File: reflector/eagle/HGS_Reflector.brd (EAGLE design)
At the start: 100 x 100 mm, 27 parts, among them J1 U.FL, U3 LP2985XX-N

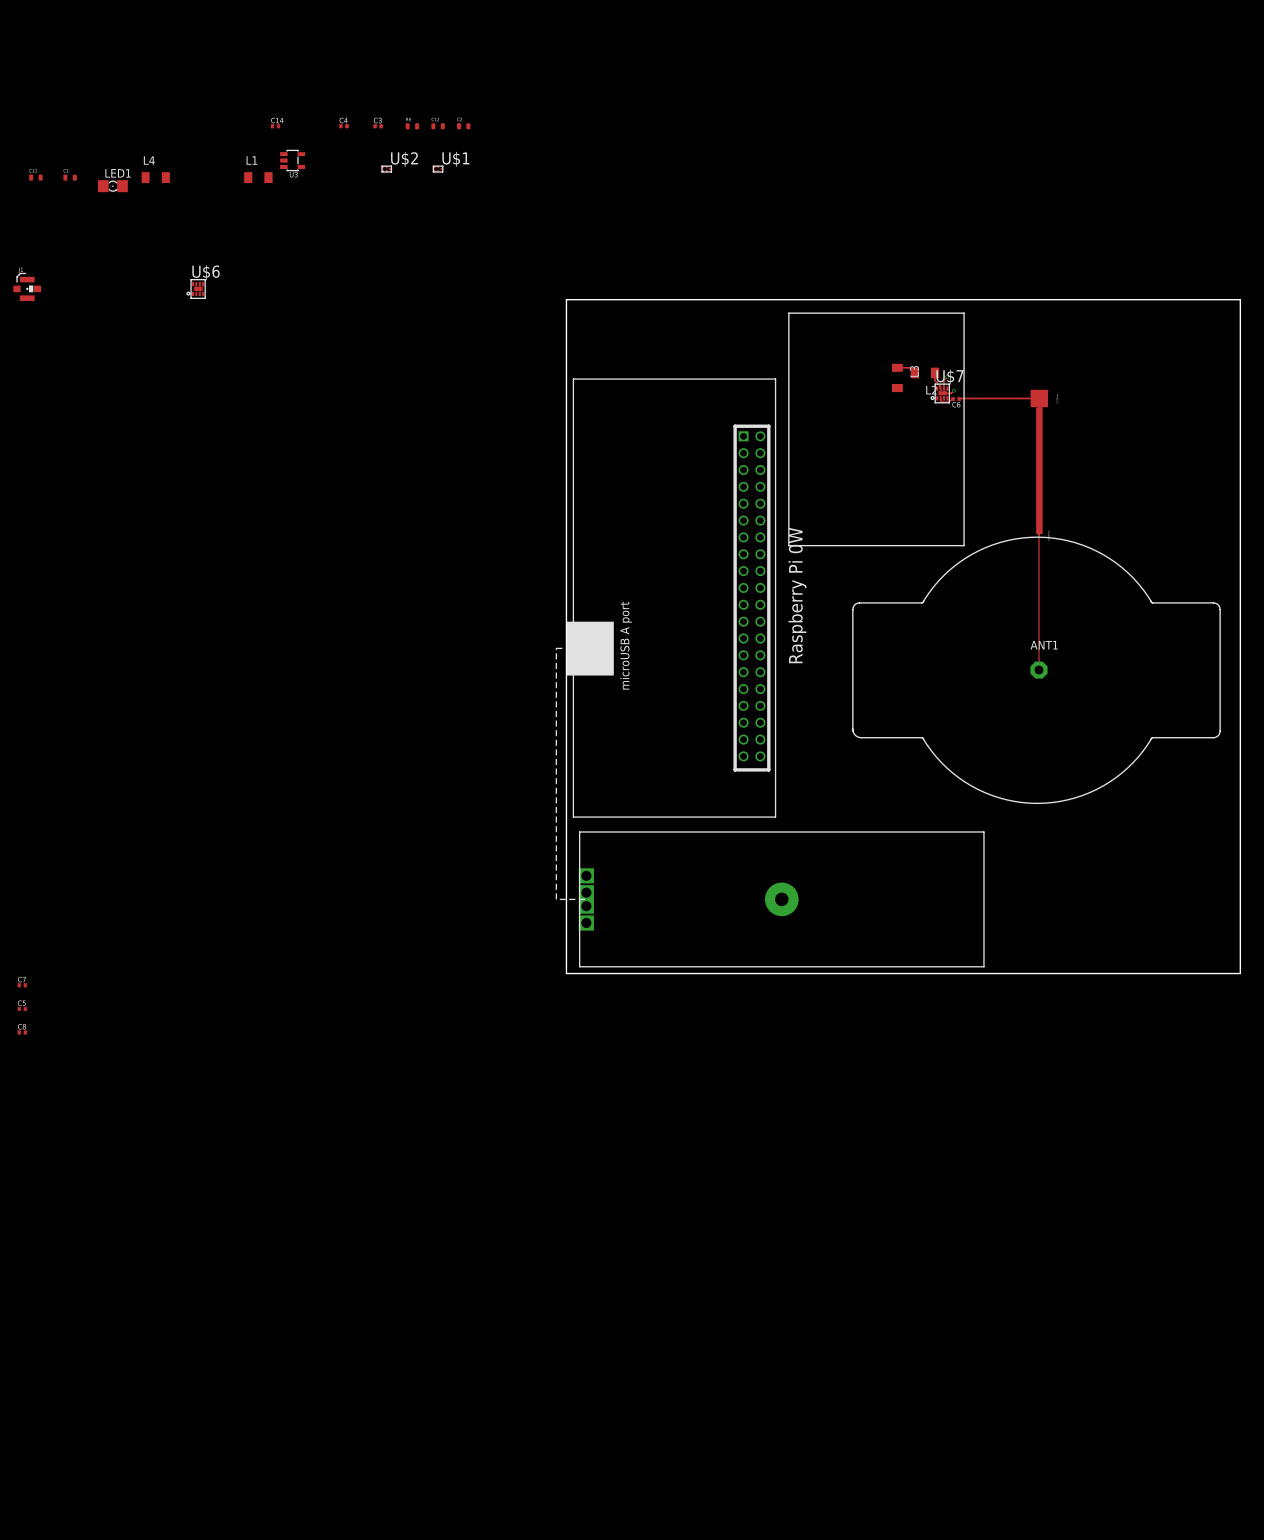
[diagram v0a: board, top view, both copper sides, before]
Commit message: Last Thursday, I updated the HGS board to its actual shape by importing the the DXF file that Marvin Lin sent me. I began work on re-routing the board to fit within the DXF dimensions.
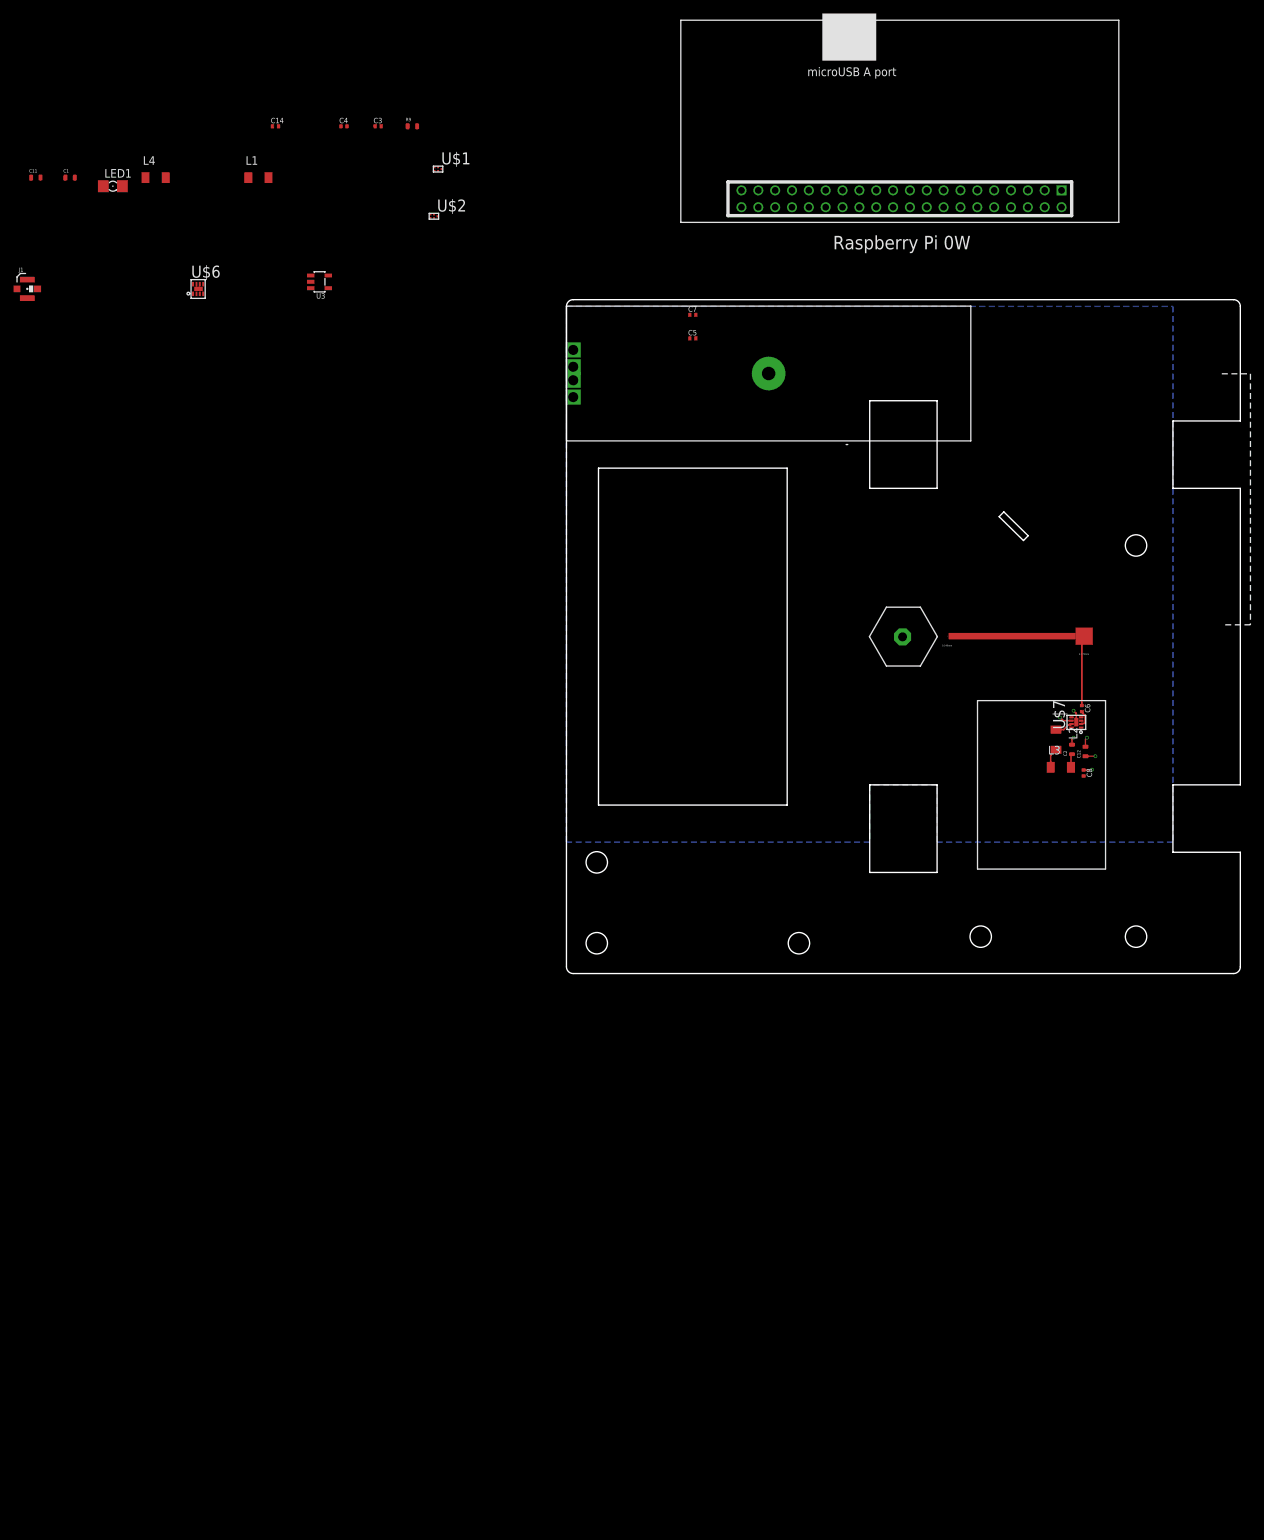
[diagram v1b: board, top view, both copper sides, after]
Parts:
- moved C8 162.1 mm to (76.8, 29.8), turned to 270 degrees
- moved C5 140.7 mm to (18.8, 94.2)
- moved C7 140.7 mm to (18.8, 97.8)
- moved C12 133.6 mm to (77.0, 33.0), turned to 90 degrees
- moved C2 129.2 mm to (75.0, 33.3), turned to 90 degrees
- moved U$5 78.3 mm to (49.5, 126.5), turned to 180 degrees
- moved U$4 78.1 mm to (30.0, 89.0)
- moved L3 62.7 mm to (73.4, 30.6), turned to 0 degrees
- moved L2 57.8 mm to (72.6, 34.7), turned to 270 degrees
- moved U$7 52.7 mm to (75.7, 37.3), turned to 90 degrees
- moved C6 49.6 mm to (76.5, 39.3), turned to 270 degrees
- moved U$3 24.9 mm to (66.1, 50.1), turned to 180 degrees
- moved ANT1 20.8 mm to (49.9, 50.0), flipped to the bottom, turned to 180 degrees
- moved U3 18.4 mm to (-36.6, 102.7)
- moved U$2 9.90 mm to (-19.7, 112.4)
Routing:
- net N$2: track 20.2 -> 0.04 mm, vias 0 -> 1
- net 3.3V: track 0.00 -> 4.76 mm, vias 0 -> 2
- net GND: track 3.74 -> 6.33 mm, vias 2 -> 4
- net N$9: track 11.9 -> 10.4 mm
- added copper zone on layer 15, net 3V
- added copper zone on layer 16, net GND
- added copper zone on layer 2, net GND_TOP
- removed copper zone on layer 15, net GND
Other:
- outline, holes or cut-outs redrawn

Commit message: Cleanup of mechanical stuff; rotated board, imported DXF, reset the dim layer, and put grounds on all layers.
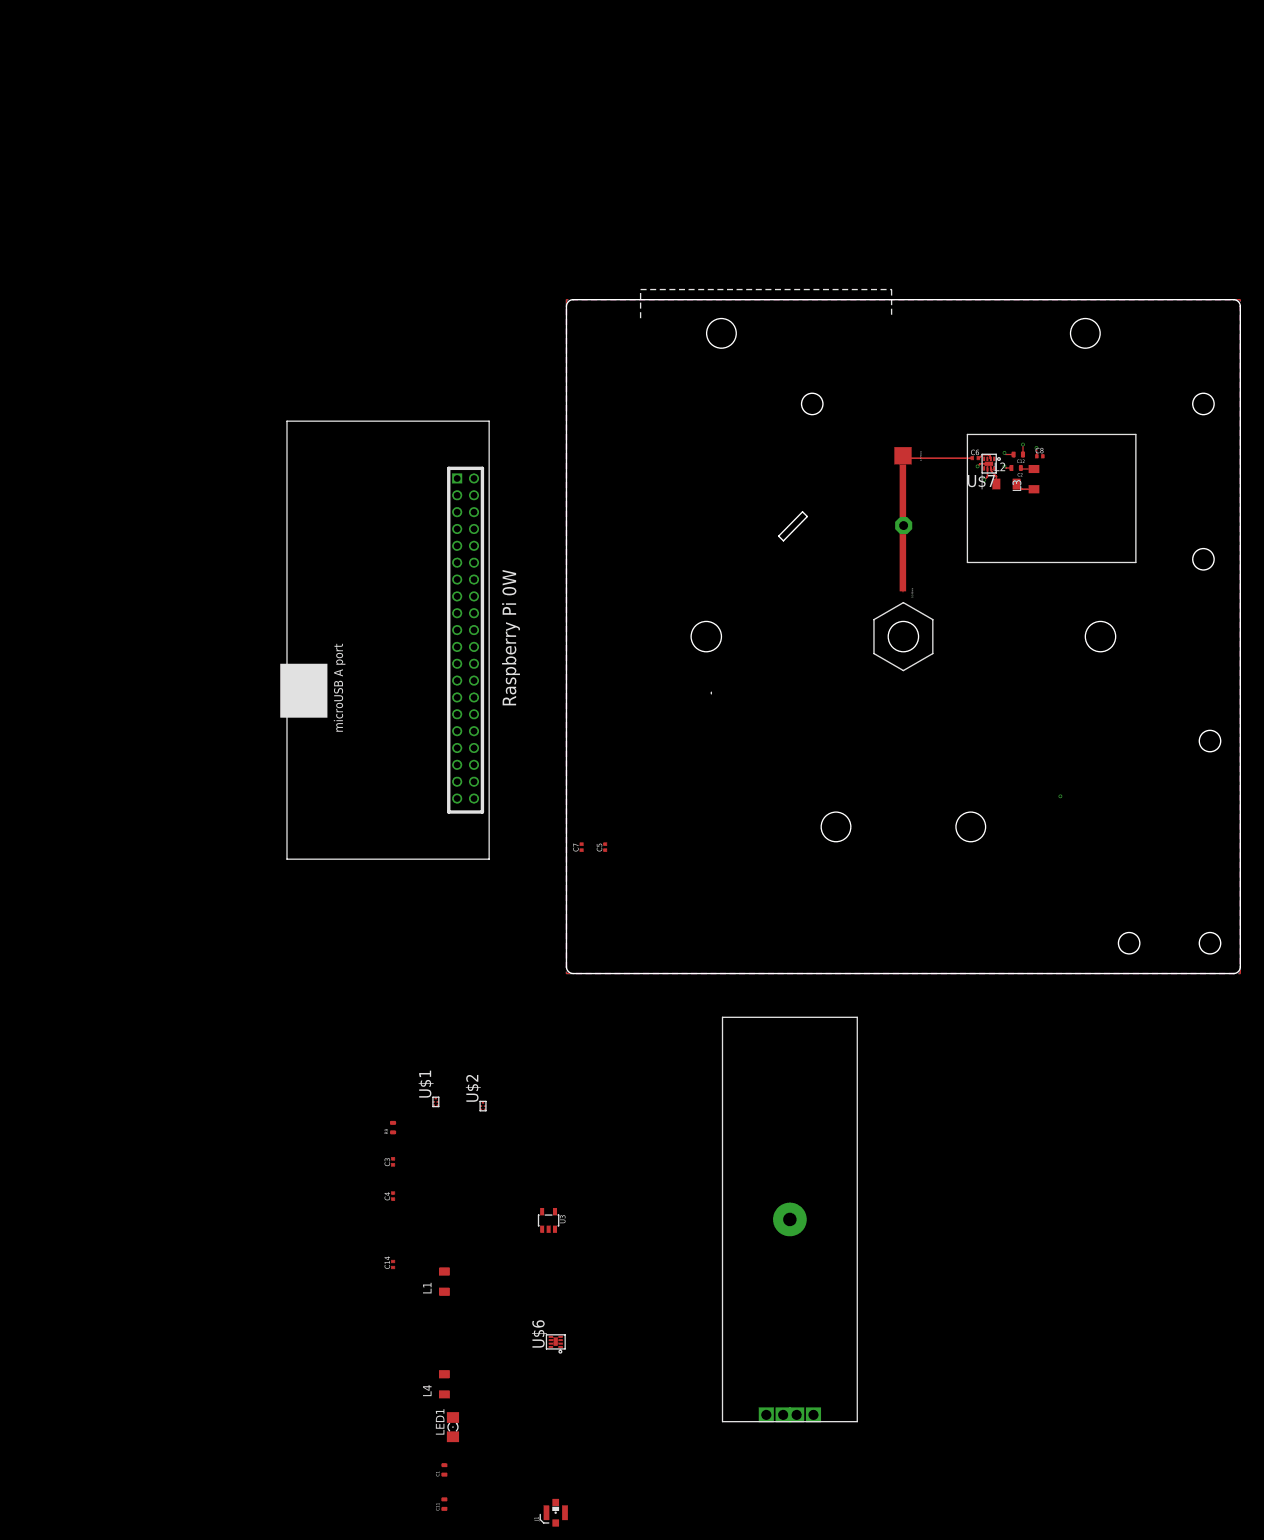
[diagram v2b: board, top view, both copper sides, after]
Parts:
- moved C11 206.0 mm to (-18.1, -78.7), turned to 90 degrees
- moved C1 199.7 mm to (-18.1, -73.7), turned to 90 degrees
- moved J1 197.8 mm to (-1.60, -80.0), turned to 90 degrees
- moved LED1 190.9 mm to (-16.8, -67.3), turned to 90 degrees
- moved L4 184.1 mm to (-18.1, -61.0), turned to 90 degrees
- moved C14 169.8 mm to (-25.7, -43.2), turned to 90 degrees
- moved L1 166.1 mm to (-18.1, -45.7), turned to 90 degrees
- moved U$6 165.0 mm to (-1.60, -54.6), turned to 90 degrees
- moved C4 158.9 mm to (-25.7, -33.0), turned to 90 degrees
- moved C3 153.7 mm to (-25.7, -27.9), turned to 90 degrees
- moved R9 148.6 mm to (-25.7, -22.9), turned to 90 degrees
- moved U3 143.4 mm to (-2.65, -36.6), turned to 90 degrees
- moved U$1 138.4 mm to (-19.4, -19.1), turned to 90 degrees
- moved U$2 132.3 mm to (-12.4, -19.7), turned to 90 degrees
- moved U$4 125.6 mm to (33.2, -36.5), turned to 0 degrees
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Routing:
- net N$2: track 0.04 -> 0.01 mm, vias 1 -> 0
- net GND: vias 4 -> 5
- added copper zone on layer 1, net GND
- added copper zone on layer 15, net GND
- added copper zone on layer 2, net GND
- removed copper zone on layer 2, net GND_TOP
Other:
- outline, holes or cut-outs redrawn

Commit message: With the DXF layer properly configured, I positioned all parts onto the board and completed all of the routing. However, there are a few DRC issues involving details of footprints that need to be changed and connections that did not route properly.
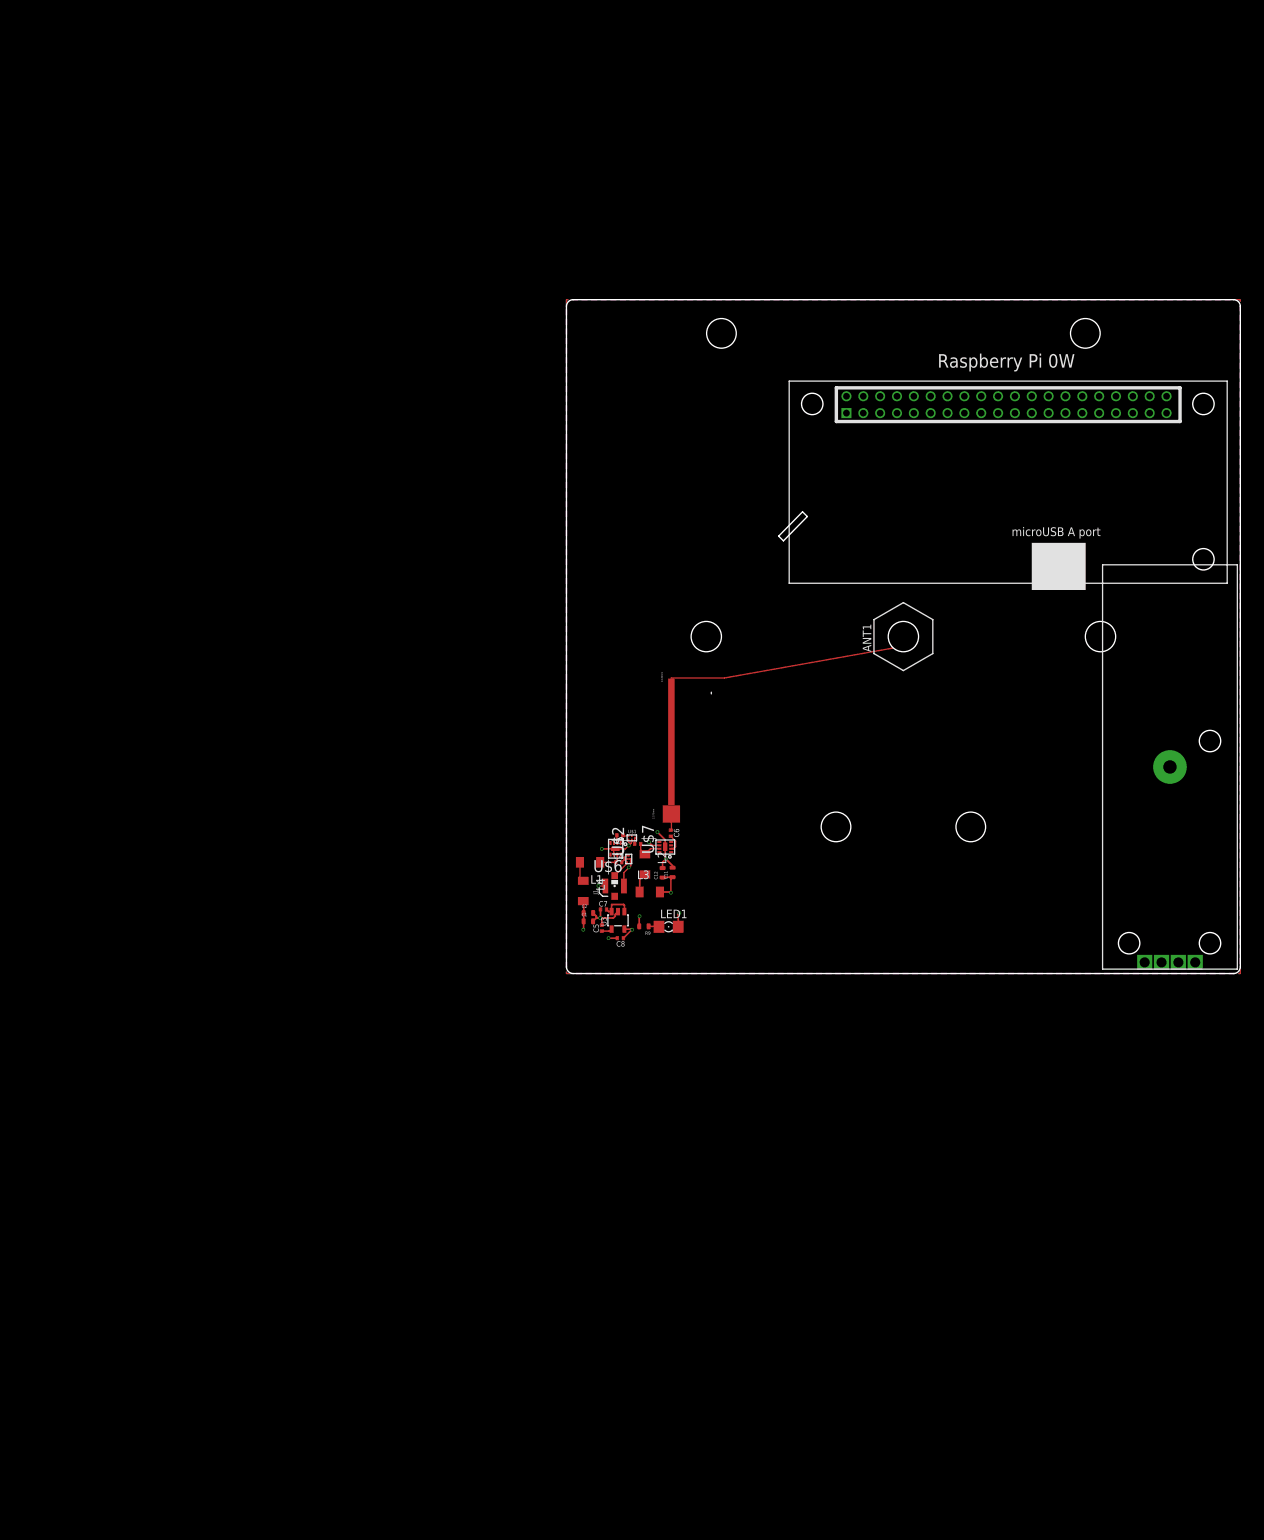
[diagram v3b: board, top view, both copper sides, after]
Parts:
- moved C11 99.7 mm to (15.8, 15.0)
- moved U$5 95.0 mm to (65.6, 72.9), turned to 0 degrees
- moved C8 94.8 mm to (8.00, 5.25), turned to 180 degrees
- moved J1 93.4 mm to (7.15, 13.0)
- moved C2 91.6 mm to (3.26, 8.98), turned to 0 degrees
- moved U$4 87.7 mm to (89.6, 30.7)
- moved C1 84.2 mm to (3.25, 7.75), turned to 0 degrees
- moved L3 83.7 mm to (12.4, 12.1), turned to 0 degrees
- moved C12 81.5 mm to (14.3, 14.9), turned to 90 degrees
- moved LED1 80.9 mm to (15.2, 6.94), turned to 0 degrees
- moved L2 77.9 mm to (11.6, 16.2), turned to 270 degrees
- moved L4 76.1 mm to (2.50, 12.2), turned to 270 degrees
- moved U$7 74.4 mm to (14.7, 18.8), turned to 90 degrees
- moved U$6 73.6 mm to (7.25, 18.5), turned to 180 degrees
- moved C14 72.2 mm to (10.6, 19.2), turned to 180 degrees
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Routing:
- net N$2: track 0.01 -> 35.6 mm
- net GND: track 6.33 -> 33.5 mm, vias 5 -> 10
- net 3.3V: track 4.76 -> 14.6 mm, vias 2 -> 4
- net N$9: track 10.4 -> 2.42 mm
- net 5V: track 0.00 -> 4.81 mm
- net N$13: track 0.00 -> 3.55 mm
- net N$14: track 0.00 -> 2.96 mm
- net N$5: track 0.00 -> 2.74 mm
- net N$3: track 0.00 -> 1.66 mm
- net N$16: track 2.65 -> 4.29 mm
- net N$1: track 0.00 -> 1.57 mm
- net N$10: track 0.00 -> 1.56 mm
- net N$8: track 0.00 -> 1.33 mm
- net N$6: track 0.00 -> 0.93 mm
- net N$4: track 0.00 -> 0.86 mm
- removed copper zone on layer 15, net 3V
